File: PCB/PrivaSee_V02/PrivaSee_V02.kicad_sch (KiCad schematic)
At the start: 20 parts, among them SW1 (Generic toggle state switch), U1 ESP32-C6-DevKitM-1, U2 LM358, U3 254, U4 DFR0568, U5 LM358

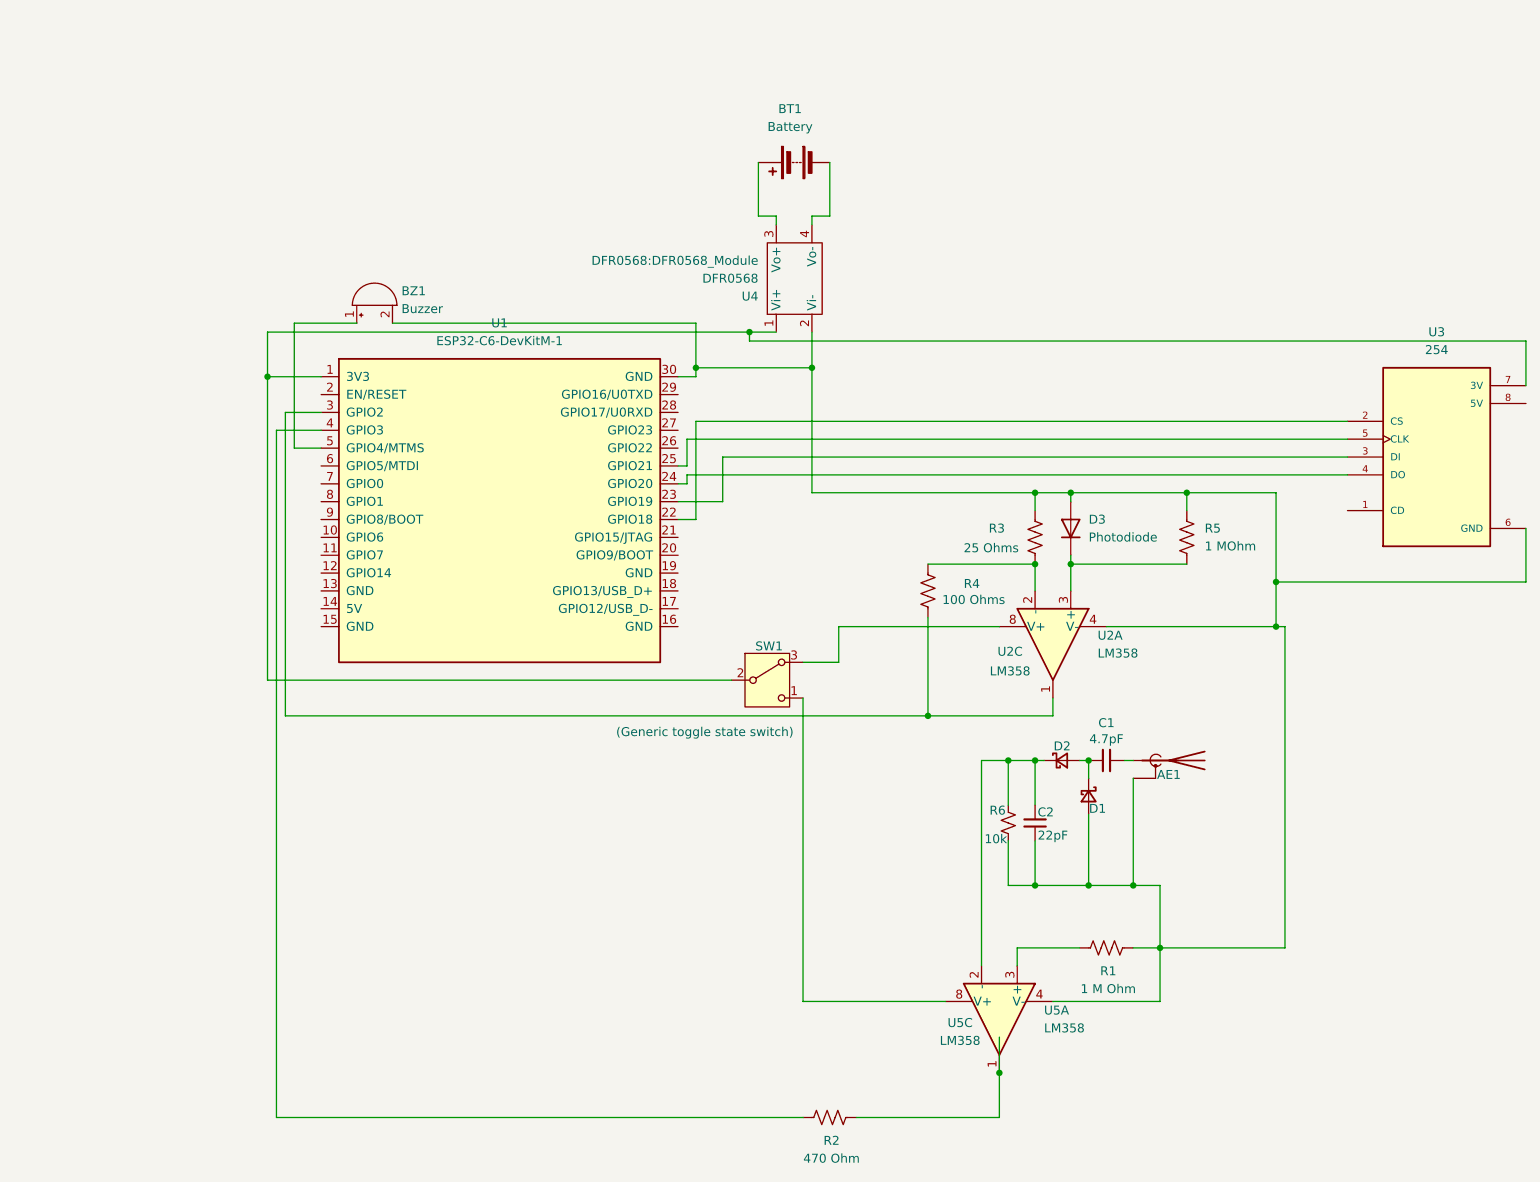
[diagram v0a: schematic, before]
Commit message: PCB Updates
Added a V2 where it was a true KiCAD Project, as well as syncing the schematic and PCB
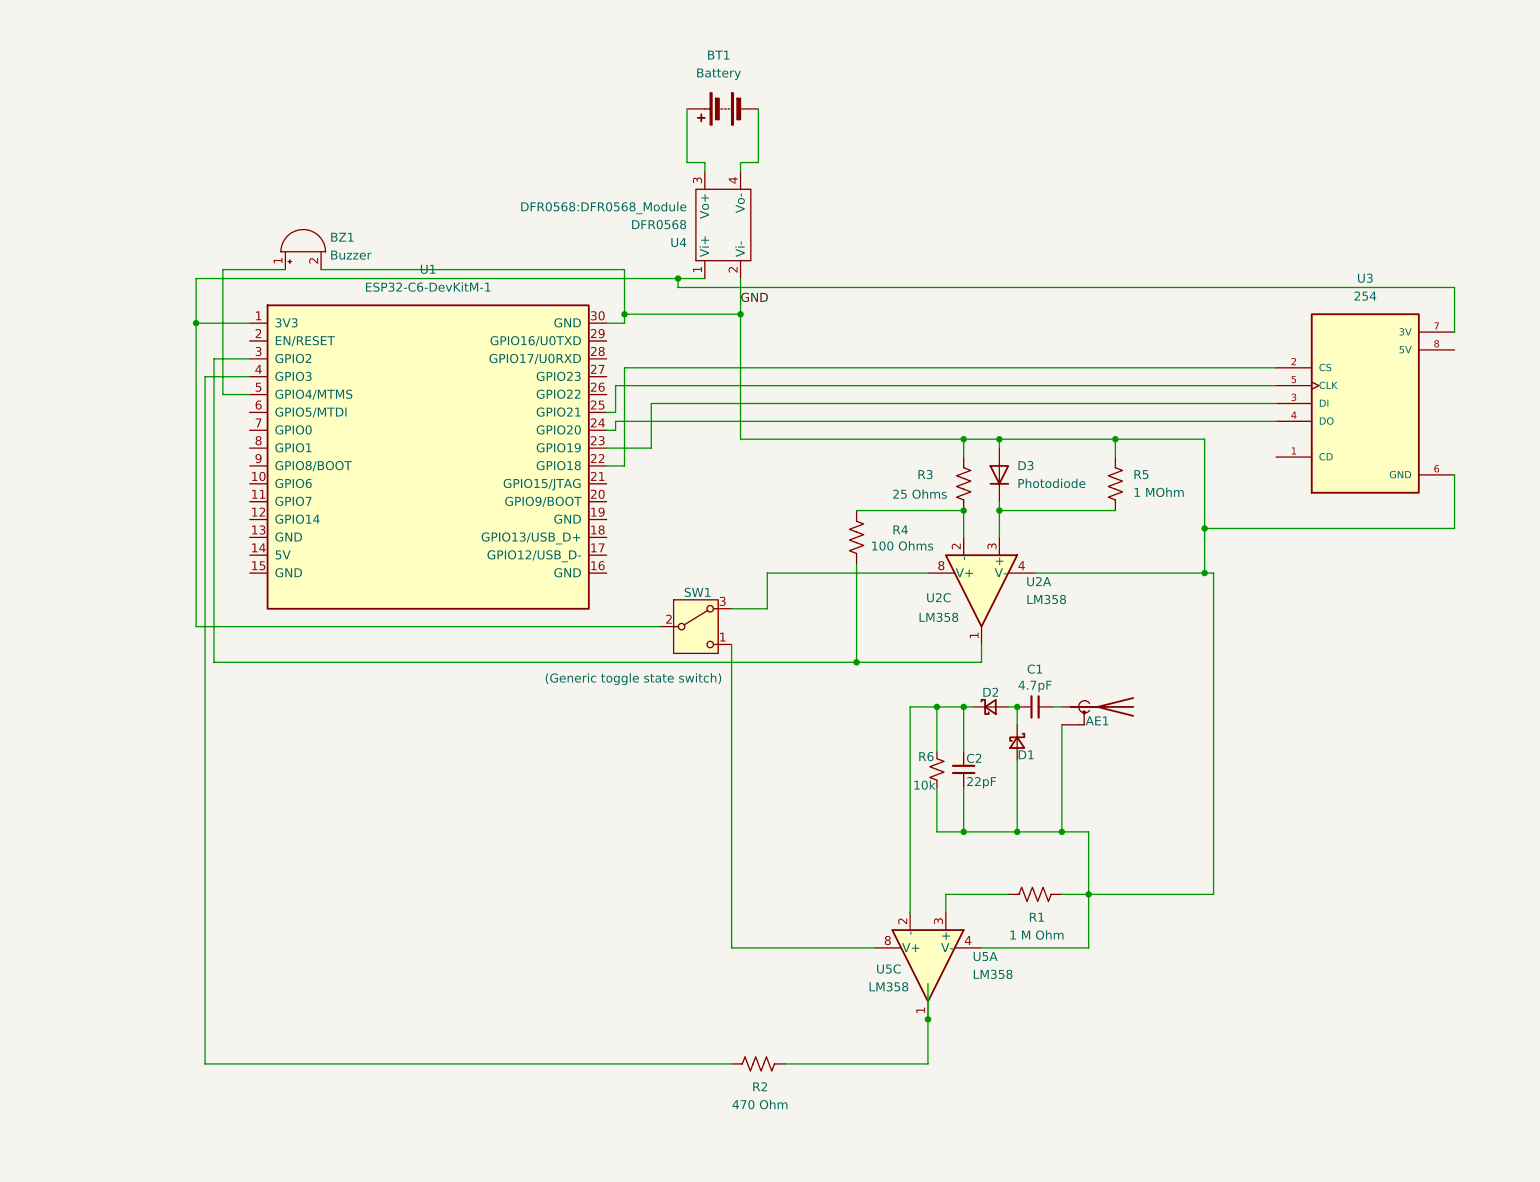
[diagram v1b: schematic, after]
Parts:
- AE1: footprint (none) -> RF_Antenna:Molex_47948-0001_2.4Ghz
- D1, D2: footprint (none) -> Diode_SMD:D_0402_1005Metric_Pad0.77x0.64mm_HandSolder
- R1, R2, R3, R4, R5: footprint Resistor_THT:R_Array_SIP4 -> Resistor_SMD:R_1218_3246Metric_Pad1.22x4.75mm_HandSolder
- R6: footprint (none) -> Resistor_SMD:R_0402_1005Metric_Pad0.72x0.64mm_HandSolder
- U1: footprint PCM_Espressif:ESP32-C6-DevKitM-1 -> RF_Module:ESP32-C3-DevKitM-1
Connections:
- net GND: now reaches AE1.2 (Shield), BZ1.2 (-), C2.1, D1.2 (A), D3.2 (A), R1.2, R3.1, R5.1, R6.2, U1.30 (GND), U2.4 (V-), U3.6 (GND), U4.2 (Vi-), U5.4 (V-)

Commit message: PCB Layout Updates
Updated the footprint and the layout of the PCB
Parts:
- added J2: Batt_Solder_Point, Connector_PinHeader_2.54mm:PinHeader_1x02_P2.54mm_Vertical, symbol Connector:Conn_01x02_Pin
- AE1: footprint RF_Antenna:Molex_47948-0001_2.4Ghz -> RF_Antenna:Johanson_2450AT18x100_2400-2500Mhz
- R1, R2, R3, R4, R5: footprint Resistor_SMD:R_1218_3246Metric_Pad1.22x4.75mm_HandSolder -> Resistor_SMD:R_1206_3216Metric_Pad1.30x1.75mm_HandSolder
- U3: footprint MicroSDCard:MODULE_254 -> Connector_PinHeader_2.54mm:PinHeader_1x08_P2.54mm_Vertical
- U4: footprint DFR0568:DFR0568_Module -> Connector_PinSocket_2.54mm:PinSocket_2x02_P2.54mm_Vertical
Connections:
- net GND: now also U1.15 (GND), U1.16 (GND), U4.4 (Vo-); no longer U4.2 (Vi-)
- net at SW1.2 (B), U1.1 (3V3), U3.7 (3V): now also U4.3 (Vo+); no longer U4.1 (Vi+)
- net at BT1.1 (+): now also U4.1 (Vi+), J2.2 (Batt+); no longer U4.3 (Vo+)
- net at BT1.2 (-): now also U4.2 (Vi-), J2.1 (Batt-); no longer U4.4 (Vo-)
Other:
- moved on the sheet: BT1

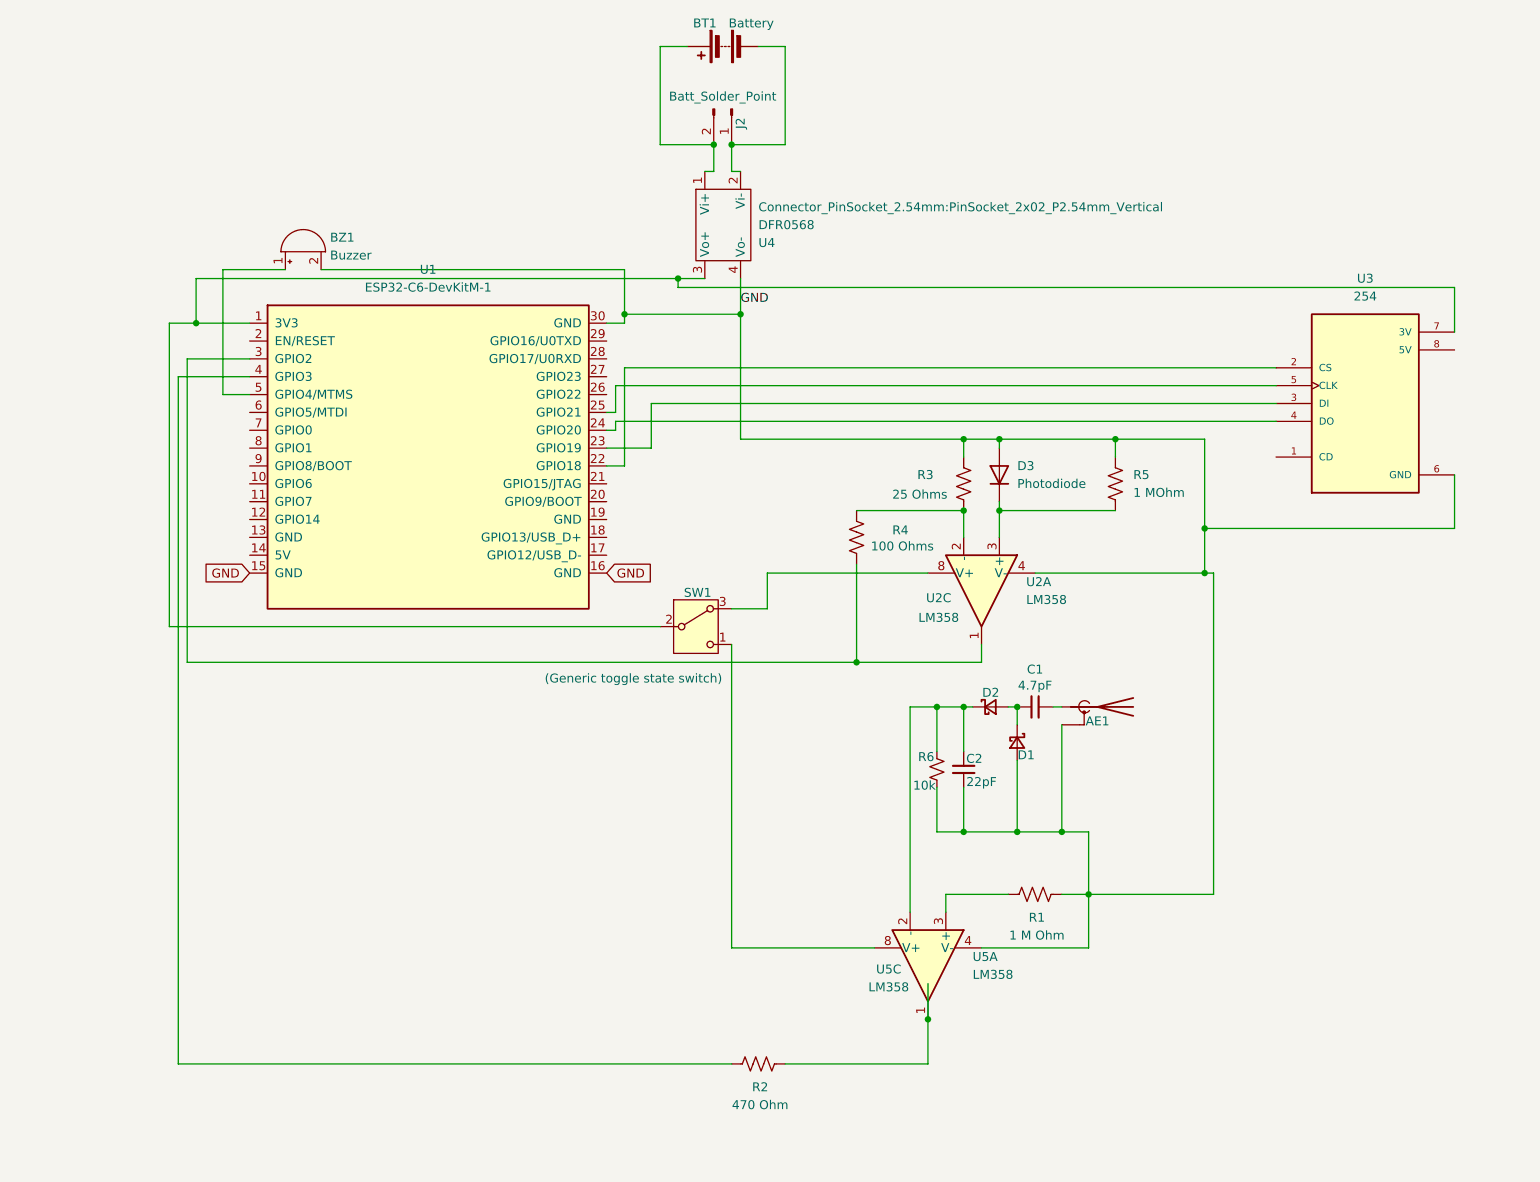
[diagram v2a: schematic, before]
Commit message: PCB Updates
Changed ESP32 to C5, reoriented all components to hopefully reduce noise, and switched to 4 layers.
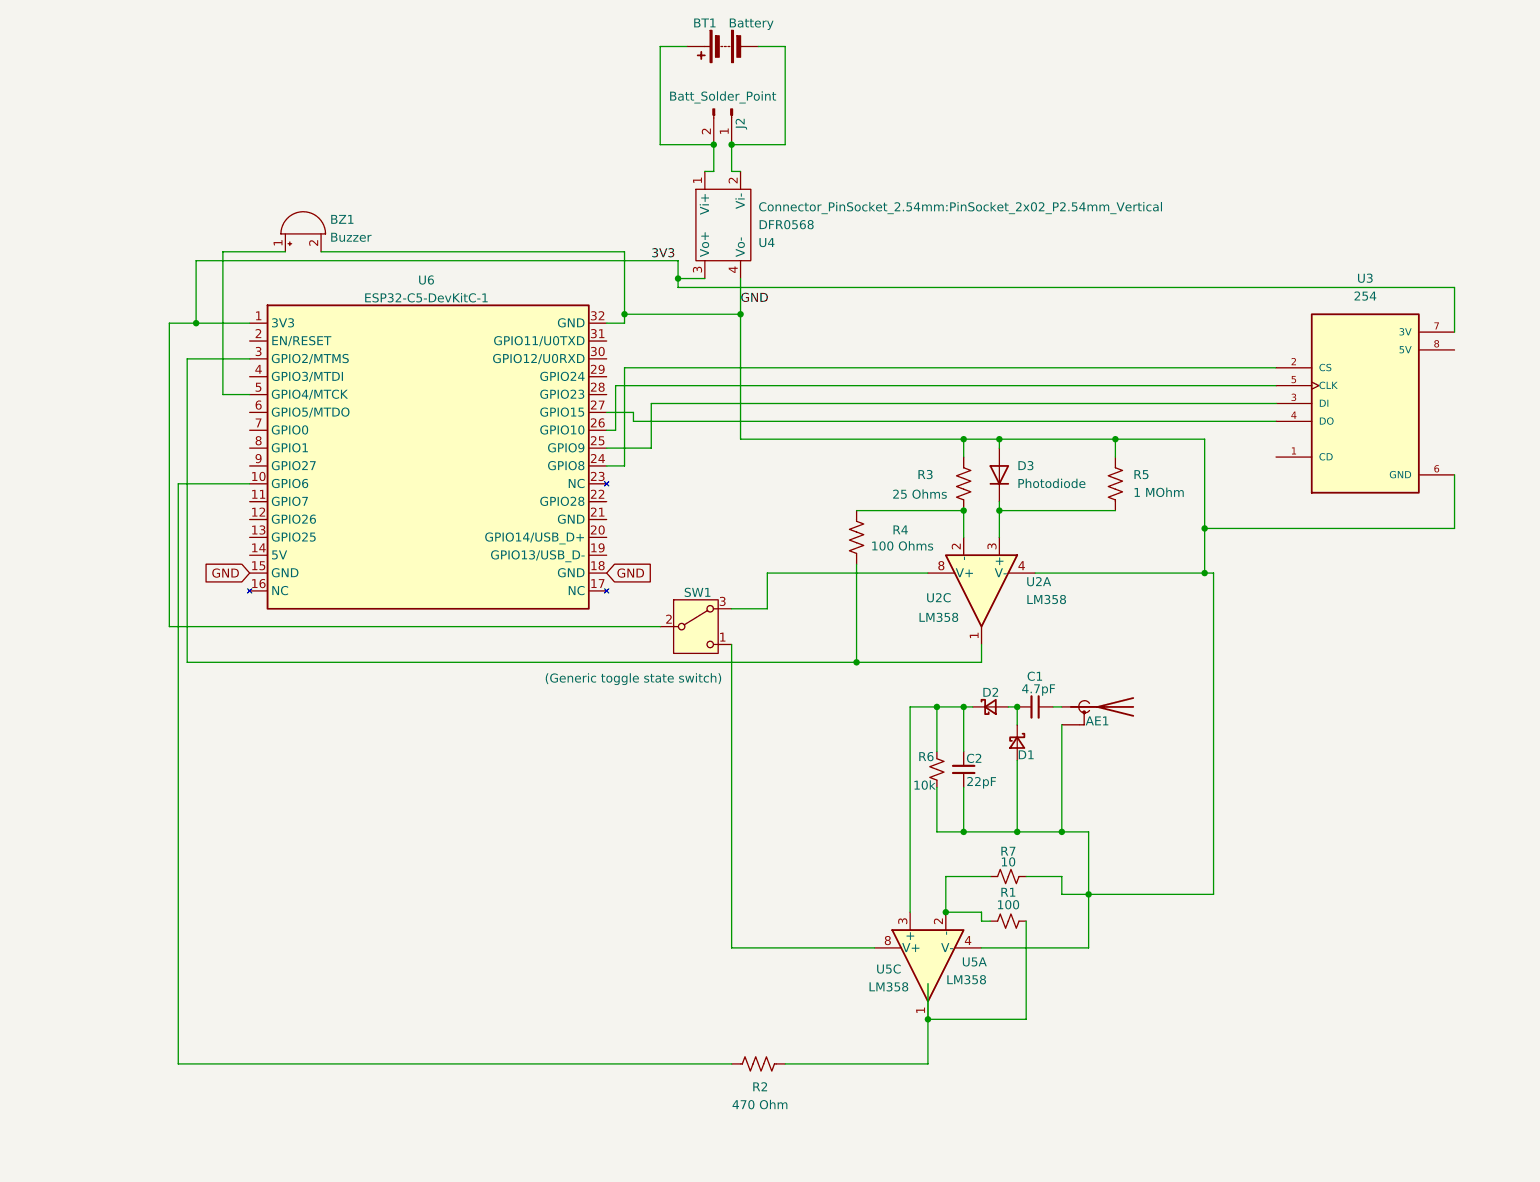
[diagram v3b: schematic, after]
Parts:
- removed R1: 1 M Ohm, Resistor_SMD:R_1206_3216Metric_Pad1.30x1.75mm_HandSolder, symbol Device:R_US
- removed U1: ESP32-C6-DevKitM-1, RF_Module:ESP32-C3-DevKitM-1, symbol PCM_Espressif:ESP32-C6-DevKitM-1
- added R1: 100, Resistor_SMD:R_1206_3216Metric_Pad1.30x1.75mm_HandSolder, symbol Device:R_Small_US
- added R7: 10, Resistor_SMD:R_1206_3216Metric_Pad1.30x1.75mm_HandSolder, symbol Device:R_Small_US
- added U6: ESP32-C5-DevKitC-1, PCM_Espressif:ESP32-C5-DevKitC-1, symbol PCM_Espressif:ESP32-C5-DevKitC-1
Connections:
- net GND: now also R7.2, U6.15 (GND), U6.18 (GND), U6.32 (GND)
- net at R4.2, U2.1: now also U6.3 (GPIO2/MTMS)
- net at R2.2, U5.1: now also R1.2
- net at C2.2, D2.1 (K), R6.1: now also U5.3 (+); no longer U5.2 (-)
- net at R2.1: now also U6.10 (GPIO6)
- net at BZ1.1 (+): now also U6.5 (GPIO4/MTCK)
- net 3V3: now reaches SW1.2 (B), U3.7 (3V), U4.3 (Vo+)
- net 3V3: now also U6.1 (3V3)
- net at U3.2 (CS): now also U6.24 (GPIO8)
- net at U3.3 (DI): now also U6.25 (GPIO9)
- net at U3.4 (DO): now also U6.27 (GPIO15)
- net at U3.5 (CLK): now also U6.26 (GPIO10)
- new net: R1.1, R7.1, U5.2 (-)
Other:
- moved on the sheet: BZ1, U5A
